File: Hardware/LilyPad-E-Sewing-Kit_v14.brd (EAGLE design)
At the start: 51.1 x 52 mm, 45 parts

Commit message: updated brd file
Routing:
- net S$10: track 18.6 -> 19.9 mm
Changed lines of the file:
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@@
 <setting verticaltext="up"/>
 </settings>
-<grid distance="0.001" unitdist="inch" unit="inch" style="lines" multiple="1" display="yes" altdistance="0.0001" altunitdist="inch" altunit="inch"/>
+<grid distance="0.05" unitdist="inch" unit="inch" style="lines" multiple="1" display="yes" altdistance="0.005" altunitdist="inch" altunit="inch"/>
 <layers>
 <layer number="1" name="Top" color="4" fill="1" visible="yes" active="yes"/>
@@
 <layer number="45" name="Holes" color="7" fill="1" visible="yes" active="yes"/>
 <layer number="46" name="Milling" color="3" fill="1" visible="yes" active="yes"/>
-<layer number="47" name="Measures" color="7" fill="1" visible="no" active="yes"/>
+<layer number="47" name="Measures" color="7" fill="1" visible="yes" active="yes"/>
 <layer number="48" name="Document" color="7" fill="1" visible="yes" active="yes"/>
 <layer number="49" name="Reference" color="11" fill="1" visible="yes" active="yes"/>
@@
 </signal>
 <signal name="S$4">
-<wire x1="12.1158" y1="44.831" x2="12.1158" y2="40.894" width="0.8128" layer="1"/>
-<wire x1="12.1158" y1="40.894" x2="20.2438" y2="40.894" width="0.8128" layer="1"/>
-<wire x1="20.2438" y1="40.894" x2="22.9108" y2="38.227" width="0.8128" layer="1"/>
-<wire x1="22.9108" y1="38.227" x2="22.9108" y2="31.242" width="0.8128" layer="1"/>
+<wire x1="12.1158" y1="44.831" x2="12.1158" y2="41.021" width="0.8128" layer="1"/>
+<wire x1="12.1158" y1="41.021" x2="20.2438" y2="41.021" width="0.8128" layer="1"/>
+<wire x1="20.2438" y1="41.021" x2="23.1648" y2="38.1" width="0.8128" layer="1"/>
+<wire x1="23.1648" y1="38.1" x2="23.1648" y2="31.115" width="0.8128" layer="1"/>
 </signal>
 <signal name="S$10">
-<wire x1="11.9888" y1="41.021" x2="4.2418" y2="41.021" width="0.8128" layer="1"/>
+<wire x1="13.2588" y1="41.021" x2="4.2418" y2="41.021" width="0.8128" layer="1"/>
 <wire x1="4.2418" y1="41.021" x2="1.0668" y2="37.846" width="0.8128" layer="1"/>
 <wire x1="1.0668" y1="37.846" x2="1.0668" y2="34.671" width="0.8128" layer="1"/>

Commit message: Updated Resistor Value
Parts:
- R4, R5, R6: value 180 -> 150

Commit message: Updated files
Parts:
- added E$1: (no value), SparkFun-Aesthetics:CREATIVE_COMMONS
- added E$2: (no value), SparkFun-Aesthetics:REVISION
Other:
- board text added: "All Units inches"
- board text added: "Board Thickness: 0.032""
- board text added: "Mary West"

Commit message: Updated Brd and Sch files (in Sync)
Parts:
- removed BUTTON-2, BUTTONS2, SLIDEOFF2, SLIDEON2: SEWTAP8, LilyPad-Wearables:PETAL-MEDIUM-2SIDE
- removed E$1: (no value), SparkFun-Aesthetics:CREATIVE_COMMONS
- removed E$2: (no value), SparkFun-Aesthetics:REVISION
- removed E$3: (no value), SparkFun-Electromechanical:BATTCON_20MM_4LEGS_OVERPASTE
- removed E$4: (no value), SparkFun-Electromechanical:AYZ0202
- removed E$5: (no value), LilyPad-Wearables:LOGO-LILYPAD
- removed JP1, JP2: FIDUCIAL1X2, SparkFun:FIDUCIAL-1X2
- removed LOGO1, LOGO2, LOGO3, LOGO4, LOGO5: LOGO-LPL, LilyPad-Wearables:LOGO-L
- removed R4, R5, R6: 150, SparkFun:0603-RES
- removed U$10, U$16, U$17, U$9: MOUSE-BITE-12_HOLES, Testing:MOUST-BITE-1-(2_HOLES)
- removed U$11, U$12, U$13, U$14: SEWTAP6, LilyPad-Wearables:PETAL-SMALL-2SIDE
- removed U$15: LOGO-LPLP, LilyPad-Wearables:LOGO-LILYPAD
- added BAT1: 20mm coincell, SparkFun-Electromechanical:BATTCON_20MM_4LEGS
- added BATB-, BATB-2, BATT+, BATT+2: SEWTAP6, LilyPad-Wearables:PETAL-SMALL-2SIDE
- added BUTTON-, BUTTONS, SLIDEOFF, SLIDEON: SEWTAP8, LilyPad-Wearables:PETAL-MEDIUM-2SIDE
- added FRAME1: FRAME-LETTER, SparkFun-Aesthetics:CREATIVE_COMMONS
- added MB+, MB-, MB1, MB10, MB2, MB3, MB4, MB5, MB6, MB7, MB8, MB9: MOUSE-BITE-12_HOLES, Testing:MOUST-BITE-1-(2_HOLES)
- added R1, R2, R3: 150, SparkFun-Resistors:0603-RES
- added S1: (no value), SparkFun-Electromechanical:AYZ0202
- LED1, LED2, LED3: value White -> WHITE; device SparkFun-3-2-07:LED-1206 -> SparkFun-LED:LED-1206
- S2: value AYZ0202 -> SWITCH-MOMENTARY-2SMD; device SparkFun:AYZ0202 -> SparkFun-Electromechanical:TACTILE-SWITCH-SMD
- S3: device SparkFun:TACTILE_SWITCH_SMD -> SparkFun-Electromechanical:AYZ0202
- U$1: value MOUSE-BITE-12_HOLES -> REVISION; device Testing:MOUST-BITE-1-(2_HOLES) -> SparkFun-Aesthetics:REVISION
- U$2, U$3: value MOUSE-BITE-12_HOLES -> (none); device Testing:MOUST-BITE-1-(2_HOLES) -> LilyPad-Wearables:LOGO-LILYPAD
- U$4, U$7, U$8: value MOUSE-BITE-12_HOLES -> (none); device Testing:MOUST-BITE-1-(2_HOLES) -> LilyPad-Wearables:LOGO-L-TINY
- U$5, U$6: value MOUSE-BITE-12_HOLES -> (none); device Testing:MOUST-BITE-1-(2_HOLES) -> LilyPad-Wearables:LOGO-L
- moved U$7 39.1 mm to (25.0, 9.94), turned to 0 degrees
- moved U$6 36.6 mm to (47.8, 35.5)
- moved U$1 35.9 mm to (0.14, -12.4), flipped to the top, turned to 0 degrees
- moved U$5 32.3 mm to (37.7, 35.9)
- moved U$2 26.9 mm to (12.8, 10.7), flipped to the top, turned to 0 degrees
- moved U$3 23.9 mm to (16.1, 36.1), turned to 0 degrees
- moved U$4 23.1 mm to (43.1, 9.96)
- moved U$8 20.4 mm to (34.2, 9.97)
- moved S2 14.3 mm to (47.8, 35.6), turned to 180 degrees
- moved LED1 13.1 mm to (43.2, 9.92)
- moved LED-1 13.0 mm to (43.2, 5.49)
- moved LED+1 13.0 mm to (43.2, 13.8)
- moved S3 5.93 mm to (37.6, 35.6), turned to 270 degrees
- moved LED2 4.82 mm to (34.3, 9.96)
- moved LED+2 4.79 mm to (34.3, 13.9)
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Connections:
- removed net BUTTON2: BUTTONS2.1, S3.2, U$8.P$1
- removed net GND2: U$11.1, U$13.1
- removed net N$4: LED1.C, R4.1
- removed net N$5: LED2.C, R5.1
- removed net N$6: LED3.C, R6.1
- removed net S$16: LED+2.1, LED2.A
- removed net S$2: U$14.1
- removed net S$25: U$2.P$1
- removed net S$26: LED+1.1, LED1.A, U$3.P$1
- removed net S$5: LED-3.1, R6.2, U$4.P$1
- removed net S$6: LED-1.1, R4.2
- removed net S$7: LED-2.1, R5.2, U$5.P$1
- removed net S$8: LED+3.1, LED3.A
- removed net SINK1: S2.4
- removed net SINK2: S2.1
- removed net SWITCH2: S2.2, S2.5, SLIDEOFF2.1, U$9.P$1
- removed net VCC2: BUTTON-2.1, S2.3, S2.6, S3.4, SLIDEON2.1, U$10.P$1, U$7.P$1
- new net BUTTON: BUTTONS.1, LED+1.1, LED1.A, MB3.P$1, MB9.P$1, S2.1
- new net GND: BAT1.NEGATIVE, BATB-.1, BATB-2.1, LED-1.1, LED-2.1, LED-3.1, MB-.P$1, MB6.P$1, MB7.P$1, MB8.P$1, R1.2, R2.2, R3.2
- new net N$1: BAT1.POSITIVE@1, BAT1.POSITIVE@2, BAT1.POSITIVE@3, BAT1.POSITIVE@4, S1.2
- new net N$11: LED1.C, R1.1
- new net N$12: LED2.C, R2.1
- new net N$13: LED3.C, R3.1
- new net N$2: BATT+.1, BATT+2.1, BUTTON-.1, MB+.P$1, MB1.P$1, S1.1, S2.3, S3.1, SLIDEON.1
- new net SWITCH: LED+2.1, LED+3.1, LED2.A, LED3.A, MB10.P$1, MB4.P$1, MB5.P$1, S3.2, SLIDEOFF.1
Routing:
- net GND: track 0.00 -> 100.4 mm
- net N$2: track 0.00 -> 65.7 mm
- net SWITCH: track 0.00 -> 48.0 mm
- net N$1: track 0.00 -> 44.2 mm, vias 0 -> 4
- net VCC2: track 34.4 -> 0.00 mm
- net BUTTON: track 0.00 -> 28.3 mm
- net S$2: track 25.6 -> 0.00 mm
- net GND2: track 25.2 -> 0.00 mm
- net S$4: track 23.1 -> 0.00 mm
- net S$10: track 19.9 -> 0.00 mm, vias 2 -> 0
- net S$29: track 19.2 -> 0.00 mm
- net SWITCH2: track 17.7 -> 0.00 mm
- net S$18: track 17.1 -> 0.00 mm
- net S$28: track 16.1 -> 0.00 mm
- net S$23: track 11.3 -> 0.00 mm
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- removed copper zone on layer 1, net GND2
- removed copper zone on layer 1, net SINK1
- removed copper zone on layer 1, net SINK2
- removed copper zone on layer 1, net VCC2
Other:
- board size 51.1 x 52 mm -> 51.4 x 52 mm
- board text added: "All Units Inches"
- board text added: "Board Thickness: "0.032""
- board text added: "M. West"
- board text removed: "All Units inches"
- board text removed: "Board Thickness: 0.032""
- board text removed: "Mary West"
- board text removed: "OFF"
- board text removed: "ON"
- board text removed: "Off"
- board text removed: "On"
- board text removed: "White"
- board text removed: "v14"

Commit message: Chnages per QC checklist
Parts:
- added FD1, FD2: FIDUCIALUFIDUCIAL, SparkFun-Aesthetics:MICRO-FIDUCIAL
- added LOGO1: SFE_LOGO_FLAME.1COP, SparkFun-Aesthetics:SFE_LOGO_FLAME_COPPER_.1
- added LOGO2: OSHW-LOGOS, SparkFun-Aesthetics:OSHW-LOGO-S
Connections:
- net N$2: now also MB2.P$1
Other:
- board text added: "v14"
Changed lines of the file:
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@@
 <setting verticaltext="up"/>
 </settings>
-<grid distance="0.01" unitdist="inch" unit="inch" style="lines" multiple="1" display="yes" altdistance="0.005" altunitdist="inch" altunit="inch"/>
+<grid distance="0.05" unitdist="inch" unit="inch" style="lines" multiple="1" display="yes" altdistance="0.005" altunitdist="inch" altunit="inch"/>
 <layers>
 <layer number="1" name="Top" color="4" fill="1" visible="yes" active="yes"/>
@@
 <text x="61.9887" y="48.16601875" size="1.778" layer="47" font="vector" ratio="15">All Units Inches</text>
 <text x="63.248540625" y="40.586659375" size="1.778" layer="51" font="vector" ratio="15">Board Thickness: "0.032"</text>
+<text x="6.35" y="0" size="1.27" layer="16" font="vector" ratio="15" rot="MR0">v14</text>
 </plain>
 <attributes>
@@
 <element name="U$5" library="LilyPad-Wearables" package="LOGO-L" value="" x="37.652959375" y="35.86988125" rot="MR0"/>
 <element name="U$6" library="LilyPad-Wearables" package="LOGO-L" value="" x="47.84344375" y="35.48888125" rot="MR0"/>
+<element name="LOGO1" library="SparkFun-Aesthetics" package="SFE_LOGO_FLAME_COPPER_.1" value="SFE_LOGO_FLAME.1COP" x="12.446" y="46.101" rot="MR0"/>
+<element name="LOGO2" library="SparkFun-Aesthetics" package="OSHW-LOGO-S" value="OSHW-LOGOS" x="21.971" y="47.371" rot="MR0"/>
+<element name="FD1" library="SparkFun-Aesthetics" package="MICRO-FIDUCIAL" value="FIDUCIALUFIDUCIAL" x="49.53" y="49.53"/>
+<element name="FD2" library="SparkFun-Aesthetics" package="MICRO-FIDUCIAL" value="FIDUCIALUFIDUCIAL" x="2.54" y="1.27"/>
 </elements>
 <signals>
@@
 <wire x1="47.8155" y1="38.54958125" x2="47.8155" y2="39.814503125" width="0.254" layer="1"/>
 <wire x1="47.8155" y1="39.814503125" x2="47.792640625" y2="39.8373625" width="0.254" layer="1"/>
+<contactref element="MB2" pad="P$1"/>
+<wire x1="37.632640625" y1="45.6184" x2="37.6301" y2="45.0596" width="0" layer="19" extent="1-1"/>
 </signal>
 <signal name="GND">

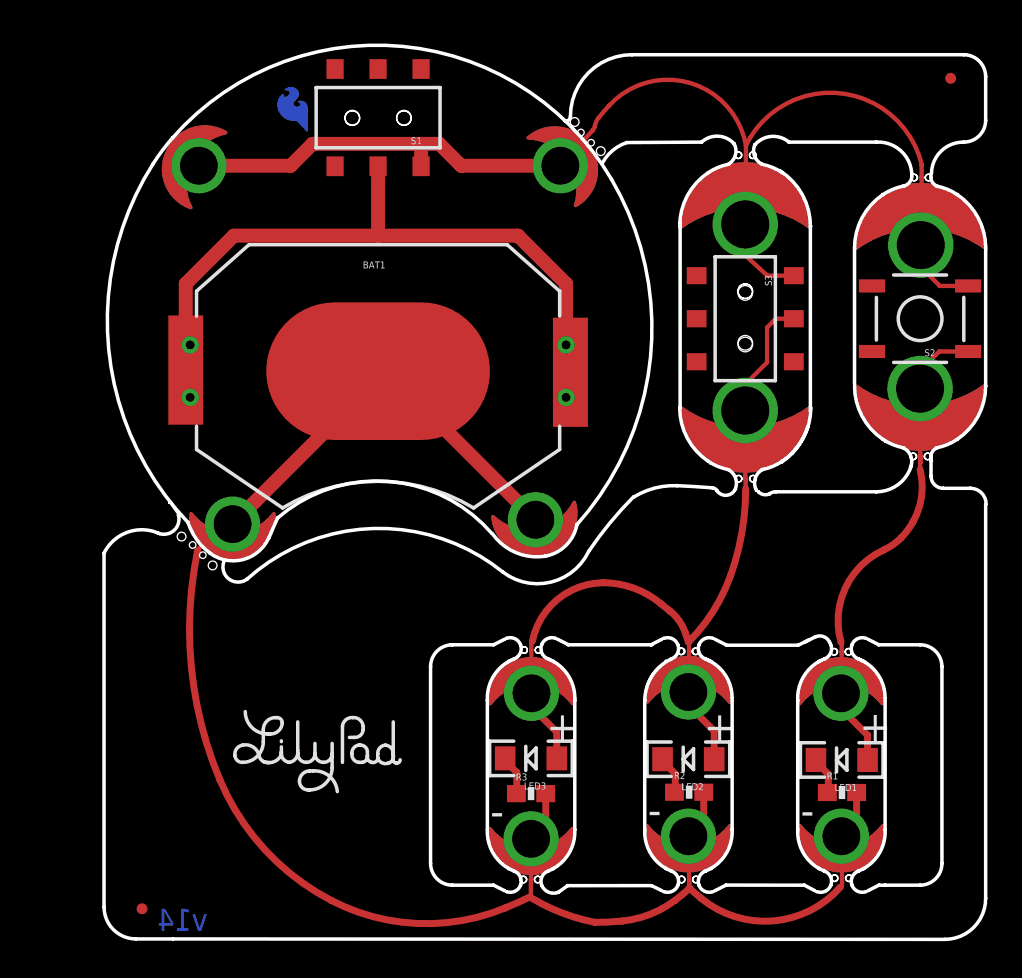
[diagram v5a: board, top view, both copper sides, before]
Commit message: updated brd files per QC
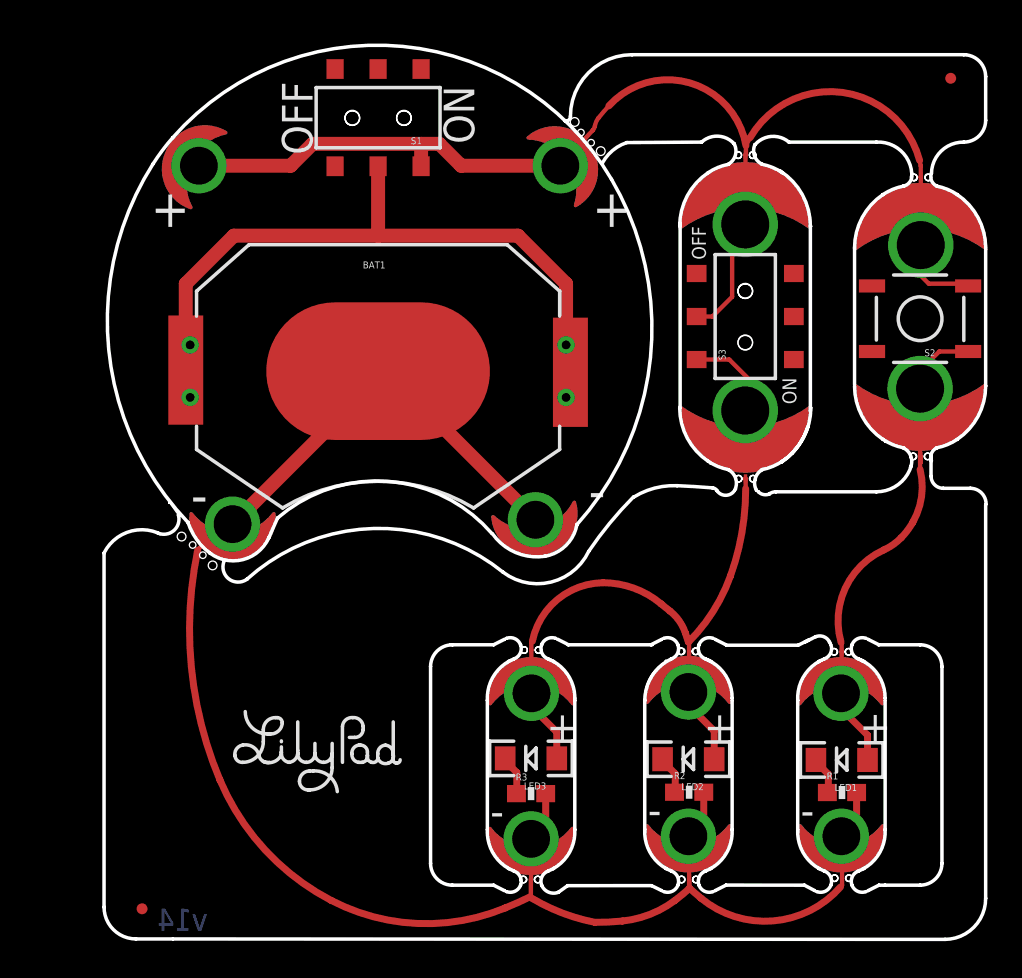
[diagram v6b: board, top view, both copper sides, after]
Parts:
- LOGO1: value SFE_LOGO_FLAME.1COP -> SFE_LOGO_FLAME.1_INCH; device SparkFun-Aesthetics:SFE_LOGO_FLAME_COPPER_.1 -> SparkFun-Aesthetics:SFE_LOGO_FLAME_.1
- moved MB1 10.3 mm to (37.6, 45.1)
- moved MB2 10.2 mm to (47.8, 43.8)
- moved S3 0.13 mm to (37.6, 35.7), turned to 90 degrees
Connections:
- new net N$3: S3.1, SLIDEOFF.1
- net N$2: now also S3.2; no longer S3.1
- net SWITCH: no longer S3.2, SLIDEOFF.1
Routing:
- net SWITCH: track 48.0 -> 36.9 mm
- net N$3: track 0.00 -> 5.66 mm
- net N$2: track 65.7 -> 68.0 mm
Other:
- board text added: "OFF"
- board text added: "ON"
- board text added: "Swicthed Coin Cell Battery Holder"

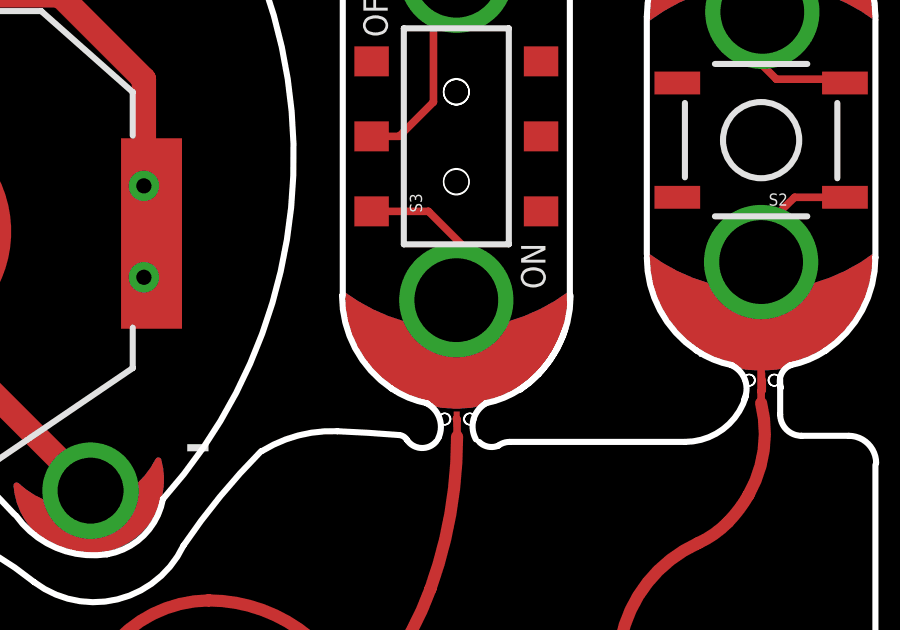
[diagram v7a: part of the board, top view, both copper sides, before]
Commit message: Updated schematic and board files --missing connection fixed
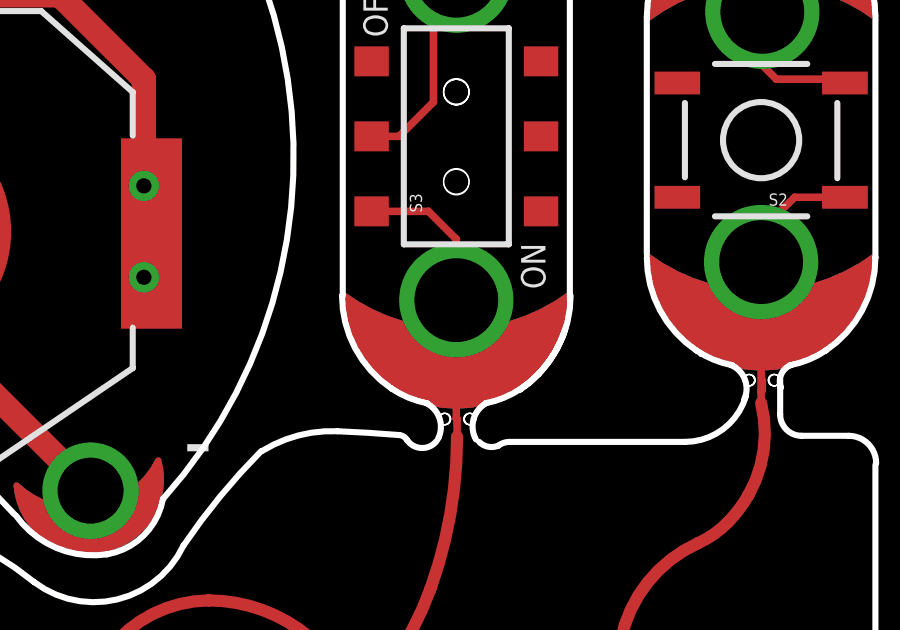
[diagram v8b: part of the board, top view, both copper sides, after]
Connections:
- removed net N$3: S3.1, SLIDEOFF.1
- net SWITCH: now also S3.1, SLIDEOFF.1
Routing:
- net SWITCH: track 36.9 -> 46.1 mm
- net N$3: track 5.66 -> 0.00 mm
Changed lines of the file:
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@@
 <contactref element="LED+3" pad="1"/>
 <contactref element="LED3" pad="A"/>
-<wire x1="37.592" y1="26.2763" x2="37.6047" y2="26.2636" width="0.254" layer="1"/>
 <wire x1="37.6047" y1="26.2636" x2="37.6174" y2="26.2509" width="0.254" layer="1"/>
 <wire x1="37.6174" y1="26.2509" x2="37.6174" y2="25.6794" width="0.254" layer="1"/>
@@
 <wire x1="25.17901875" y1="12.99971875" x2="25.17901875" y2="13.78458125" width="0.4064" layer="1"/>
 <wire x1="25.17901875" y1="13.78458125" x2="25.1714" y2="13.7922" width="0.4064" layer="1"/>
+<contactref element="S3" pad="1"/>
+<contactref element="SLIDEOFF" pad="1"/>
+<wire x1="37.592" y1="30.226" x2="37.592" y2="26.2763" width="0.254" layer="1"/>
+<wire x1="37.592" y1="26.2763" x2="37.6047" y2="26.2636" width="0.254" layer="1"/>
+<wire x1="34.767" y1="33.187" x2="36.663" y2="33.187" width="0.254" layer="1"/>
+<wire x1="37.592" y1="30.226" x2="37.592" y2="32.258" width="0.254" layer="1"/>
+<wire x1="37.592" y1="32.258" x2="36.663" y2="33.187" width="0.254" layer="1"/>
 </signal>
 <signal name="N$11">
@@
 <wire x1="24.31541875" y1="7.98231875" x2="24.296" y2="7.9629" width="0.4064" layer="1"/>
 </signal>
-<signal name="N$3">
-<contactref element="S3" pad="1"/>
-<contactref element="SLIDEOFF" pad="1"/>
-<wire x1="34.767" y1="33.187" x2="36.663" y2="33.187" width="0.254" layer="1"/>
-<wire x1="36.663" y1="33.187" x2="38.1" y2="31.75" width="0.254" layer="1"/>
-<wire x1="38.1" y1="31.75" x2="38.1" y2="30.734" width="0.254" layer="1"/>
-<wire x1="38.1" y1="30.734" x2="37.592" y2="30.226" width="0.254" layer="1"/>
-</signal>
 </signals>
